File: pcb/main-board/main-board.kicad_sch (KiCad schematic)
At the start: 3 parts, among them J1 Conn_01x04_Socket, J2 Conn_01x04_Socket, U1 PicoW

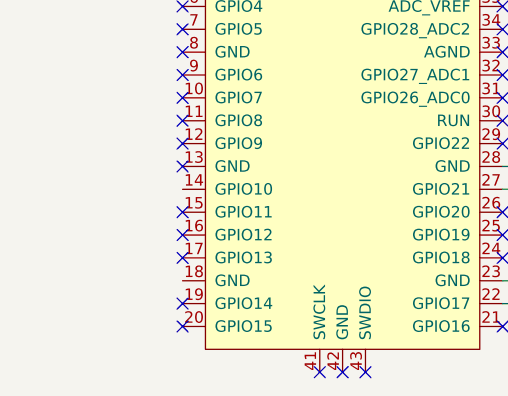
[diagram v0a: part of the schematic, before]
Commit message: Added switch
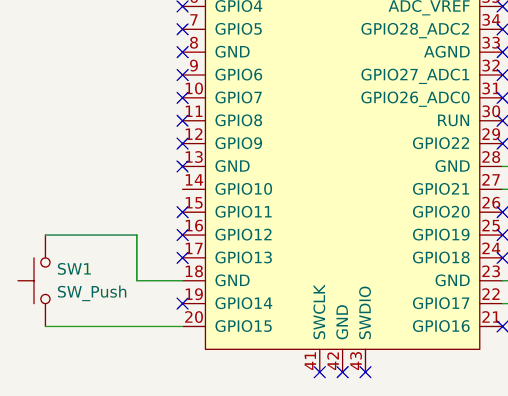
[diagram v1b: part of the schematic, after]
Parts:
- added SW1: SW_Push, RaspberryPI PicoW:Switch, symbol Switch:SW_Push
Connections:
- net at U1.18 (GND): now also SW1.2
- net at U1.20 (GPIO15): now also SW1.1
- no-connect marks 38 -> 37
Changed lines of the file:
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@@
-	)
-	(no_connect
-		(at 119.38 123.19)
 	)
 	(no_connect
@@
 	(wire
 		(pts
+			(xy 104.14 123.19) (xy 119.38 123.19)
+		)
+		(stroke
+			(width 0)
+			(type default)
+		)
+	)
+	(wire
+		(pts
 			(xy 154.94 74.93) (xy 165.1 74.93)
 		)
@@
 	(wire
 		(pts
+			(xy 104.14 113.03) (xy 114.3 113.03)
+		)
+		(stroke
+			(width 0)
+			(type default)
+		)
+	)
+	(wire
+		(pts
 			(xy 154.94 120.65) (xy 161.29 120.65)
 		)
@@
 	(wire
 		(pts
+			(xy 114.3 118.11) (xy 114.3 113.03)
+		)
+		(stroke
+			(width 0)
+			(type default)
+		)
+	)
+	(wire
+		(pts
 			(xy 154.94 107.95) (xy 161.29 107.95)
 		)
@@
 		(pts
 			(xy 165.1 123.19) (xy 165.1 107.95)
+		)
+		(stroke
+			(width 0)
+			(type default)
+		)
+	)
+	(wire
+		(pts
+			(xy 119.38 118.11) (xy 114.3 118.11)
 		)
 		(stroke
@@
 					(unit 1)
 				)
+			)
+		)
+	)
+	(symbol
+		(lib_id "Switch:SW_Push")
+		(at 104.14 118.11 90)
+		(unit 1)
+		(exclude_from_sim no)
+		(in_bom yes)
+		(on_board yes)
+		(dnp no)
+		(fields_autoplaced yes)
+		(property "Reference" "SW1"
+			(at 105.41 116.8399 90)
+			(effects
+				(font
+					(size 1.27 1.27)
+				)
+				(justify right)
+			)
+		)
+		(property "Value" "SW_Push"
+			(at 105.41 119.3799 90)
+			(effects
+				(font
+					(size 1.27 1.27)
+				)
+				(justify right)
+			)
+		)
+		(property "Footprint" "RaspberryPI PicoW:Switch"
+			(at 99.06 118.11 0)
+			(effects
+				(font
+					(size 1.27 1.27)
+				)
+				(hide yes)
+			)
+		)
+		(property "Datasheet" "~"
+			(at 99.06 118.11 0)
+			(effects
+				(font
+					(size 1.27 1.27)
+				)
+				(hide yes)
+			)
+		)
+		(property "Description" "Push button switch, generic, two pins"
+			(at 104.14 118.11 0)
+			(effects
+				(font
+					(size 1.27 1.27)
+				)
+				(hide yes)
+			)
+		)
+		(pin "1"
+		)
+		(pin "2"
+		)
+		(instances
+			(project ""
+				(path "/7d3991f7-8efb-4a32-808f-244ec6694f12"
+					(reference "SW1")
+					(unit 1)
+				)

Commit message: Added colon LEDs, moved stuff around the board, etc
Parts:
- added LED1, LED2: LED_SK6812RGBW_5050Metric_Pad1.5x1.5mm_HandSolder, RaspberryPI PicoW:LED_SK6812RGBW_5050Metric_Pad1.5x1.5mm_HandSolder, symbol Custom:LED_SK6812RGBW_5050Metric_Pad1.5x1.5mm_HandSolder
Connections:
- net at J1.4 (Pin_4), J2.4 (Pin_4), U1.40 (VBUS): now also LED1.1 (VCC), LED2.1 (VCC)
- net at U1.21 (GPIO16): now also LED1.4 (Data_IN)
- new net: LED1.2 (Data_OUT), LED2.4 (Data_IN)
- new net: LED1.3 (GND), LED2.3 (GND)
